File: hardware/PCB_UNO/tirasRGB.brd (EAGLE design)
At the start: 100 x 80 mm, 10 parts, among them IC1 MEGA8-P, IC2 LD117AV

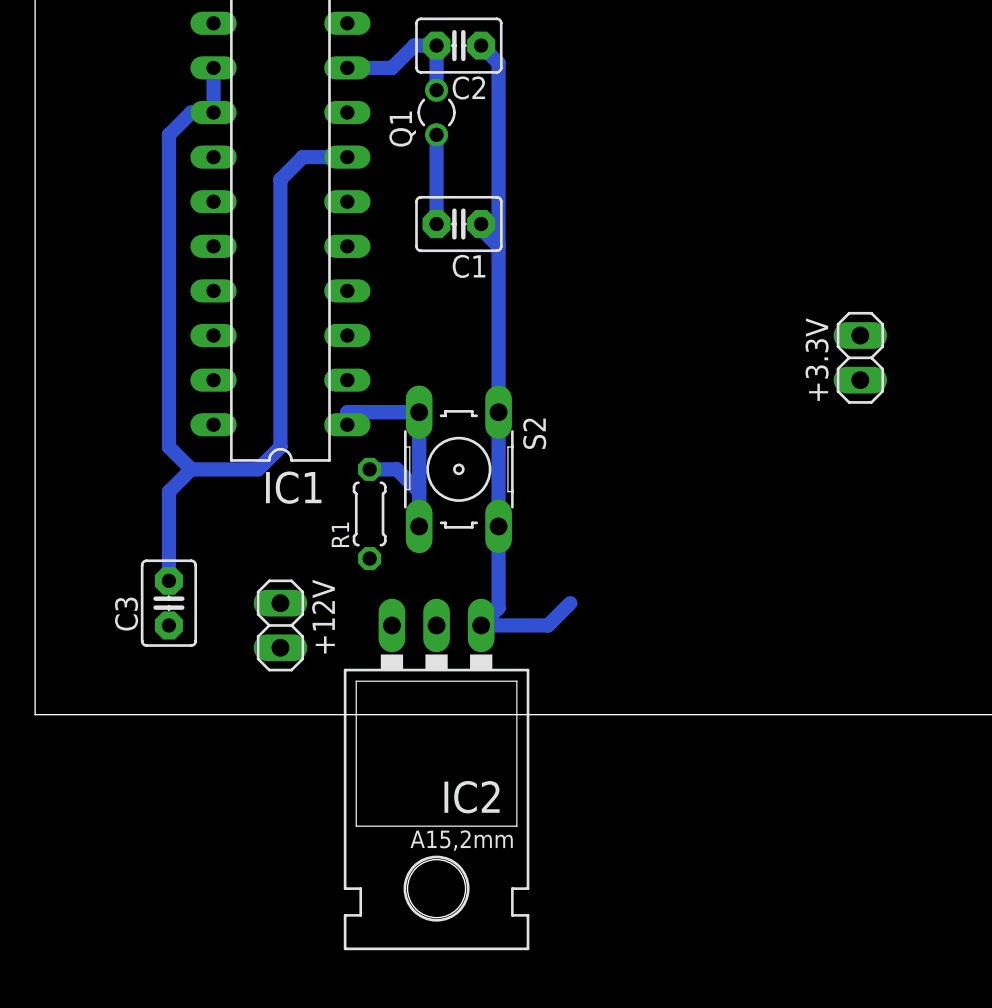
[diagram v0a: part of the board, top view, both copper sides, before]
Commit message: Se cambia regulador del diseño PCB y se eliminan ficheros generados por la impresora de PCB
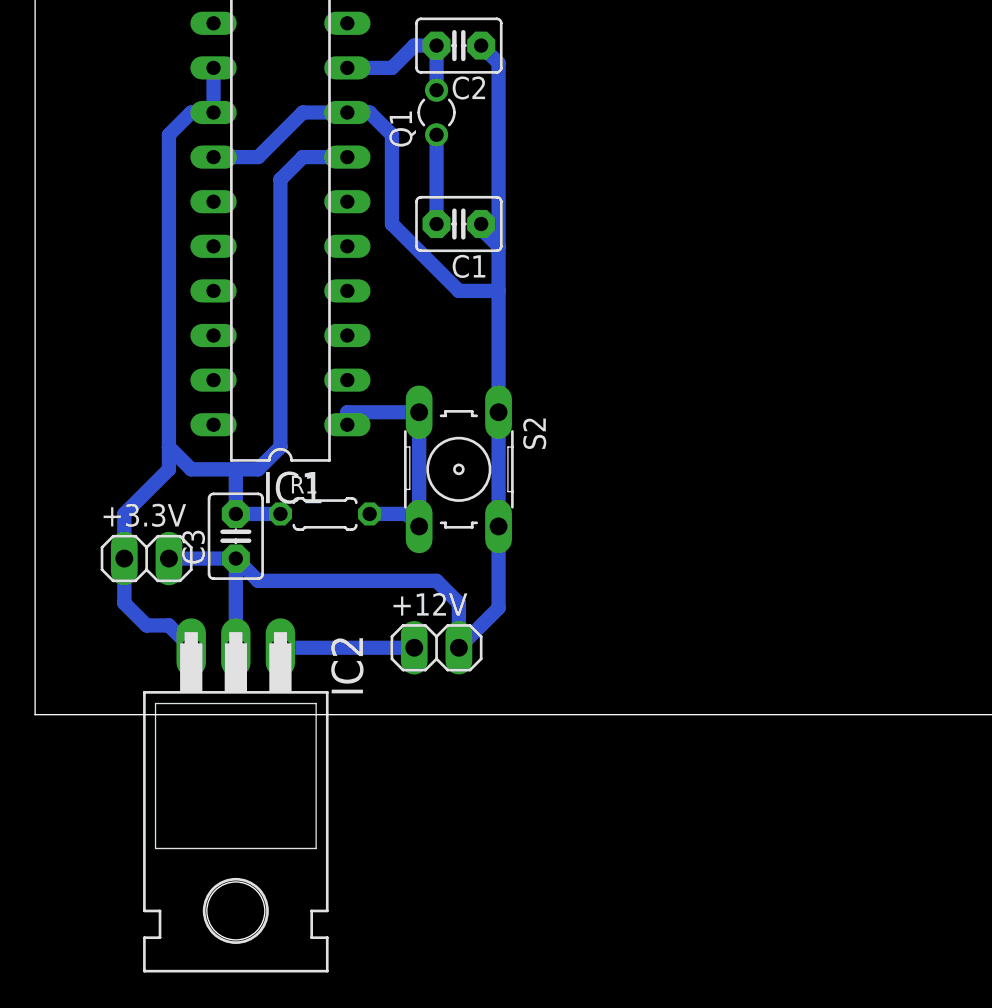
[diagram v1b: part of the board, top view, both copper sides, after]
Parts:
- IC2: value LD117AV -> 7805T; device v-reg:TO220L1 -> linear:TO220H
- moved +3.3V 42.2 mm to (6.35, 8.89), turned to 0 degrees
- moved IC2 13.7 mm to (11.4, -6.35)
- moved +12V 8.98 mm to (22.9, 3.81), turned to 0 degrees
- moved C3 5.39 mm to (11.4, 10.2)
- moved R1 2.54 mm to (16.5, 11.4), turned to 0 degrees
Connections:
- net 3.3V: now also IC2.3; no longer IC2.2
- net GND: now also +3.3V.2, IC2.2; no longer IC2.1
- net N$2: now also IC2.1; no longer IC2.3
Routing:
- net GND: track 41.1 -> 87.0 mm
- net 3.3V: track 57.2 -> 70.2 mm
- net N$2: track 0.00 -> 7.62 mm
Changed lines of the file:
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@@
 <attribute name="OC_FARNELL" value="unknown" x="41.91" y="64.77" size="1.778" layer="27" rot="R90" display="off"/>
 </element>
-<element name="R1" library="rcl" package="0204/5" value="" x="19.05" y="11.43" rot="R90"/>
+<element name="R1" library="rcl" package="0204/5" value="" x="16.51" y="11.43"/>
 <element name="Q1" library="crystal" package="TC26V" value="" x="22.86" y="34.29" rot="R90">
 <attribute name="OC_NEWARK" value="unknown" x="73.66" y="49.53" size="1.778" layer="27" rot="R90" display="off"/>
@@
 <element name="C1" library="capacitor-wima" package="C2.5-3" value="" x="24.13" y="27.94" rot="R180"/>
 <element name="C2" library="capacitor-wima" package="C2.5-3" value="" x="24.13" y="38.1" rot="R180"/>
-<element name="C3" library="capacitor-wima" package="C2.5-3" value="" x="7.62" y="6.35" rot="R90"/>
+<element name="C3" library="capacitor-wima" package="C2.5-3" value="" x="11.43" y="10.16" rot="R90"/>
 <element name="S2" library="switch-omron" package="B3F-10XX" value="" x="24.13" y="13.97" rot="R270">
 <attribute name="OC_NEWARK" value="36M3542" x="-13.97" y="-5.08" size="1.778" layer="27" rot="R270" display="off"/>
@@
 <attribute name="OC_FARNELL" value="176432" x="-13.97" y="-5.08" size="1.778" layer="27" rot="R270" display="off"/>
 </element>
-<element name="+3.3V" library="pinhead" package="1X02" value="" x="46.99" y="20.32" rot="R90"/>
-<element name="IC2" library="v-reg" package="TO220L1" value="LD117AV" x="22.86" y="1.27" rot="R180"/>
-<element name="+12V" library="pinhead" package="1X02" value="" x="13.97" y="5.08" rot="R270"/>
+<element name="+3.3V" library="pinhead" package="1X02" value="" x="6.35" y="8.89"/>
+<element name="+12V" library="pinhead" package="1X02" value="" x="22.86" y="3.81"/>
+<element name="IC2" library="linear" package="TO220H" value="7805T" x="11.43" y="-6.35" rot="R180"/>
 </elements>
 <signals>
@@
 <contactref element="S2" pad="2"/>
 <contactref element="IC1" pad="22"/>
-<contactref element="IC2" pad="1"/>
 <wire x1="26.3906" y1="10.7188" x2="26.3906" y2="17.2212" width="0.8128" layer="16"/>
-<wire x1="30.48" y1="6.35" x2="29.21" y2="5.08" width="0.8128" layer="16"/>
-<wire x1="29.21" y1="5.08" x2="25.4" y2="5.08" width="0.8128" layer="16"/>
-<wire x1="26.3906" y1="10.7188" x2="26.3906" y2="6.0706" width="0.8128" layer="16"/>
-<wire x1="26.3906" y1="6.0706" x2="25.4" y2="5.08" width="0.8128" layer="16"/>
 <contactref element="C3" pad="1"/>
 <contactref element="C2" pad="1"/>
@@
 <contactref element="IC1" pad="8"/>
 <contactref element="+12V" pad="2"/>
-<wire x1="26.3906" y1="17.2212" x2="26.3906" y2="26.67" width="0.8128" layer="16"/>
+<wire x1="26.3906" y1="17.2212" x2="26.3906" y2="24.13" width="0.8128" layer="16"/>
+<wire x1="26.3906" y1="24.13" x2="26.3906" y2="26.67" width="0.8128" layer="16"/>
 <wire x1="26.3906" y1="26.67" x2="26.3906" y2="37.1094" width="0.8128" layer="16"/>
 <wire x1="26.3906" y1="37.1094" x2="25.4" y2="38.1" width="0.8128" layer="16"/>
 <wire x1="25.4" y1="27.94" x2="25.4" y2="27.6606" width="0.8128" layer="16"/>
 <wire x1="25.4" y1="27.6606" x2="26.3906" y2="26.67" width="0.8128" layer="16"/>
-<wire x1="10.16" y1="31.75" x2="17.78" y2="34.29" width="0" layer="19" extent="1-1"/>
-<wire x1="25.4" y1="38.1" x2="17.78" y2="34.29" width="0" layer="19" extent="1-1"/>
-<wire x1="13.97" y1="3.81" x2="25.4" y2="5.08" width="0" layer="19" extent="1-1"/>
-<wire x1="7.62" y1="5.08" x2="13.97" y2="3.81" width="0" layer="19" extent="1-1"/>
+<wire x1="17.78" y1="34.29" x2="19.05" y2="34.29" width="0.8128" layer="16"/>
+<wire x1="19.05" y1="34.29" x2="20.32" y2="33.02" width="0.8128" layer="16"/>
+<wire x1="20.32" y1="33.02" x2="20.32" y2="27.94" width="0.8128" layer="16"/>
+<wire x1="20.32" y1="27.94" x2="24.13" y2="24.13" width="0.8128" layer="16"/>
+<wire x1="24.13" y1="24.13" x2="26.3906" y2="24.13" width="0.8128" layer="16"/>
+<wire x1="17.78" y1="34.29" x2="15.24" y2="34.29" width="0.8128" layer="16"/>
+<wire x1="15.24" y1="34.29" x2="12.7" y2="31.75" width="0.8128" layer="16"/>
+<wire x1="12.7" y1="31.75" x2="10.16" y2="31.75" width="0.8128" layer="16"/>
+<contactref element="+3.3V" pad="2"/>
+<contactref element="IC2" pad="2"/>
+<wire x1="24.13" y1="3.81" x2="26.3906" y2="6.0706" width="0.8128" layer="16"/>
+<wire x1="26.3906" y1="6.0706" x2="26.3906" y2="10.7188" width="0.8128" layer="16"/>
+<wire x1="11.43" y1="3.81" x2="11.43" y2="8.89" width="0.8128" layer="16"/>
+<wire x1="11.43" y1="8.89" x2="12.7" y2="7.62" width="0.8128" layer="16"/>
+<wire x1="12.7" y1="7.62" x2="22.86" y2="7.62" width="0.8128" layer="16"/>
+<wire x1="22.86" y1="7.62" x2="24.13" y2="6.35" width="0.8128" layer="16"/>
+<wire x1="24.13" y1="6.35" x2="24.13" y2="3.81" width="0.8128" layer="16"/>
+<wire x1="7.62" y1="8.89" x2="11.43" y2="8.89" width="0.8128" layer="16"/>
 </signal>
 <signal name="N$14">
@@
 <wire x1="21.8694" y1="17.2212" x2="17.78" y2="17.2212" width="0.8128" layer="16"/>
 <wire x1="17.78" y1="17.2212" x2="17.78" y2="16.51" width="0.8128" layer="16"/>
-<wire x1="21.8694" y1="10.7188" x2="21.8694" y2="12.7" width="0.8128" layer="16"/>
-<wire x1="21.8694" y1="12.7" x2="21.8694" y2="17.2212" width="0.8128" layer="16"/>
-<wire x1="19.05" y1="13.97" x2="20.5994" y2="13.97" width="0.8128" layer="16"/>
-<wire x1="20.5994" y1="13.97" x2="21.8694" y2="12.7" width="0.8128" layer="16"/>
+<wire x1="21.8694" y1="10.7188" x2="21.8694" y2="17.2212" width="0.8128" layer="16"/>
+<wire x1="19.05" y1="11.43" x2="21.1582" y2="11.43" width="0.8128" layer="16"/>
+<wire x1="21.1582" y1="11.43" x2="21.8694" y2="10.7188" width="0.8128" layer="16"/>
 </signal>
 <signal name="3.3V">
@@
 <contactref element="R1" pad="1"/>
 <wire x1="10.16" y1="36.83" x2="10.16" y2="34.29" width="0.8128" layer="16"/>
+<contactref element="C3" pad="2"/>
+<contactref element="+3.3V" pad="1"/>
 <wire x1="17.78" y1="31.75" x2="15.24" y2="31.75" width="0.8128" layer="16"/>
 <wire x1="15.24" y1="31.75" x2="13.97" y2="30.48" width="0.8128" layer="16"/>
 <wire x1="13.97" y1="30.48" x2="13.97" y2="15.24" width="0.8128" layer="16"/>
 <wire x1="13.97" y1="15.24" x2="12.7" y2="13.97" width="0.8128" layer="16"/>
-<wire x1="12.7" y1="13.97" x2="8.89" y2="13.97" width="0.8128" layer="16"/>
+<wire x1="12.7" y1="13.97" x2="11.43" y2="13.97" width="0.8128" layer="16"/>
+<wire x1="11.43" y1="13.97" x2="8.89" y2="13.97" width="0.8128" layer="16"/>
 <wire x1="8.89" y1="13.97" x2="7.62" y2="15.24" width="0.8128" layer="16"/>
 <wire x1="7.62" y1="15.24" x2="7.62" y2="33.02" width="0.8128" layer="16"/>
 <wire x1="7.62" y1="33.02" x2="8.89" y2="34.29" width="0.8128" layer="16"/>
 <wire x1="8.89" y1="34.29" x2="10.16" y2="34.29" width="0.8128" layer="16"/>
-<wire x1="15.24" y1="11.43" x2="12.7" y2="13.97" width="0" layer="19" extent="1-16"/>
-<contactref element="C3" pad="2"/>
-<wire x1="7.62" y1="7.62" x2="7.62" y2="12.7" width="0.8128" layer="16"/>
-<wire x1="7.62" y1="12.7" x2="8.89" y2="13.97" width="0.8128" layer="16"/>
-<contactref element="IC2" pad="2"/>
-<contactref element="+3.3V" pad="1"/>
-<wire x1="19.05" y1="8.89" x2="22.86" y2="5.08" width="0" layer="19" extent="1-1"/>
-<wire x1="15.24" y1="11.43" x2="19.05" y2="8.89" width="0" layer="19" extent="16-16"/>
-<wire x1="46.99" y1="19.05" x2="15.24" y2="11.43" width="0" layer="19" extent="16-16"/>
+<wire x1="11.43" y1="11.43" x2="11.43" y2="13.97" width="0.8128" layer="16"/>
+<wire x1="13.97" y1="11.43" x2="11.43" y2="11.43" width="0.8128" layer="16"/>
+<contactref element="IC2" pad="3"/>
+<wire x1="8.89" y1="3.81" x2="7.62" y2="5.08" width="0.8128" layer="16"/>
+<wire x1="7.62" y1="5.08" x2="6.35" y2="5.08" width="0.8128" layer="16"/>
+<wire x1="6.35" y1="5.08" x2="5.08" y2="6.35" width="0.8128" layer="16"/>
+<wire x1="5.08" y1="6.35" x2="5.08" y2="8.89" width="0.8128" layer="16"/>
+<wire x1="5.08" y1="8.89" x2="5.08" y2="11.43" width="0.8128" layer="16"/>
+<wire x1="5.08" y1="11.43" x2="7.62" y2="13.97" width="0.8128" layer="16"/>
+<wire x1="7.62" y1="13.97" x2="7.62" y2="15.24" width="0.8128" layer="16"/>
 </signal>
 <signal name="N$2">
-<contactref element="IC2" pad="3"/>
 <contactref element="+12V" pad="1"/>
-<wire x1="13.97" y1="6.35" x2="20.32" y2="5.08" width="0" layer="19" extent="1-1"/>
+<contactref element="IC2" pad="1"/>
+<wire x1="21.59" y1="3.81" x2="13.97" y2="3.81" width="0.8128" layer="16"/>
 </signal>
 </signals>
